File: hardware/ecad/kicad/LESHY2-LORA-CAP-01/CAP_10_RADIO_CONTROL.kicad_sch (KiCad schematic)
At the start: 0 parts

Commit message: complete H2.4.2 LoRa Cap root
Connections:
- no-connect marks 0 -> 10
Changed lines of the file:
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@@
 	(generator_version "10.0")
 	(paper "A4")
+	(hierarchical_label "CAP_3V3"
+		(shape bidirectional)
+		(at 20.32 20.32 0)
+		(effects (font (size 1.27 1.27)))
+	)
+	(wire
+		(pts (xy 20.32 20.32) (xy 25.40 20.32))
+		(stroke (width 0) (type default))
+	)
+	(no_connect (at 25.40 20.32)
+	)
+	(hierarchical_label "GND"
+		(shape bidirectional)
+		(at 20.32 25.40 0)
+		(effects (font (size 1.27 1.27)))
+	)
+	(wire
+		(pts (xy 20.32 25.40) (xy 25.40 25.40))
+		(stroke (width 0) (type default))
+	)
+	(no_connect (at 25.40 25.40)
+	)
+	(hierarchical_label "LORA_NRESET"
+		(shape bidirectional)
+		(at 20.32 30.48 0)
+		(effects (font (size 1.27 1.27)))
+	)
+	(wire
+		(pts (xy 20.32 30.48) (xy 25.40 30.48))
+		(stroke (width 0) (type default))
+	)
+	(no_connect (at 25.40 30.48)
+	)
+	(hierarchical_label "LORA_DIO1"
+		(shape bidirectional)
+		(at 20.32 35.56 0)
+		(effects (font (size 1.27 1.27)))
+	)
+	(wire
+		(pts (xy 20.32 35.56) (xy 25.40 35.56))
+		(stroke (width 0) (type default))
+	)
+	(no_connect (at 25.40 35.56)
+	)
+	(hierarchical_label "LORA_BUSY"
+		(shape bidirectional)
+		(at 20.32 40.64 0)
+		(effects (font (size 1.27 1.27)))
+	)
+	(wire
+		(pts (xy 20.32 40.64) (xy 25.40 40.64))
+		(stroke (width 0) (type default))
+	)
+	(no_connect (at 25.40 40.64)
+	)
+	(hierarchical_label "LORA_SCK"
+		(shape bidirectional)
+		(at 190.50 20.32 180)
+		(effects (font (size 1.27 1.27)) (justify right))
+	)
+	(wire
+		(pts (xy 190.50 20.32) (xy 185.42 20.32))
+		(stroke (width 0) (type default))
+	)
+	(no_connect (at 185.42 20.32)
+	)
+	(hierarchical_label "LORA_MOSI"
+		(shape bidirectional)
+		(at 190.50 25.40 180)
+		(effects (font (size 1.27 1.27)) (justify right))
+	)
+	(wire
+		(pts (xy 190.50 25.40) (xy 185.42 25.40))
+		(stroke (width 0) (type default))
+	)
+	(no_connect (at 185.42 25.40)
+	)
+	(hierarchical_label "LORA_MISO"
+		(shape bidirectional)
+		(at 190.50 30.48 180)
+		(effects (font (size 1.27 1.27)) (justify right))
+	)
+	(wire
+		(pts (xy 190.50 30.48) (xy 185.42 30.48))
+		(stroke (width 0) (type default))
+	)
+	(no_connect (at 185.42 30.48)
+	)
+	(hierarchical_label "LORA_NSS"
+		(shape bidirectional)
+		(at 190.50 35.56 180)
+		(effects (font (size 1.27 1.27)) (justify right))
+	)
+	(wire
+		(pts (xy 190.50 35.56) (xy 185.42 35.56))
+		(stroke (width 0) (type default))
+	)
+	(no_connect (at 185.42 35.56)
+	)
+	(hierarchical_label "RF_FORWARD_LEVEL"
+		(shape bidirectional)
+		(at 190.50 40.64 180)
+		(effects (font (size 1.27 1.27)) (justify right))
+	)
+	(wire
+		(pts (xy 190.50 40.64) (xy 185.42 40.64))
+		(stroke (width 0) (type default))
+	)
+	(no_connect (at 185.42 40.64)
+	)
 	(sheet_instances
 		(path "/"

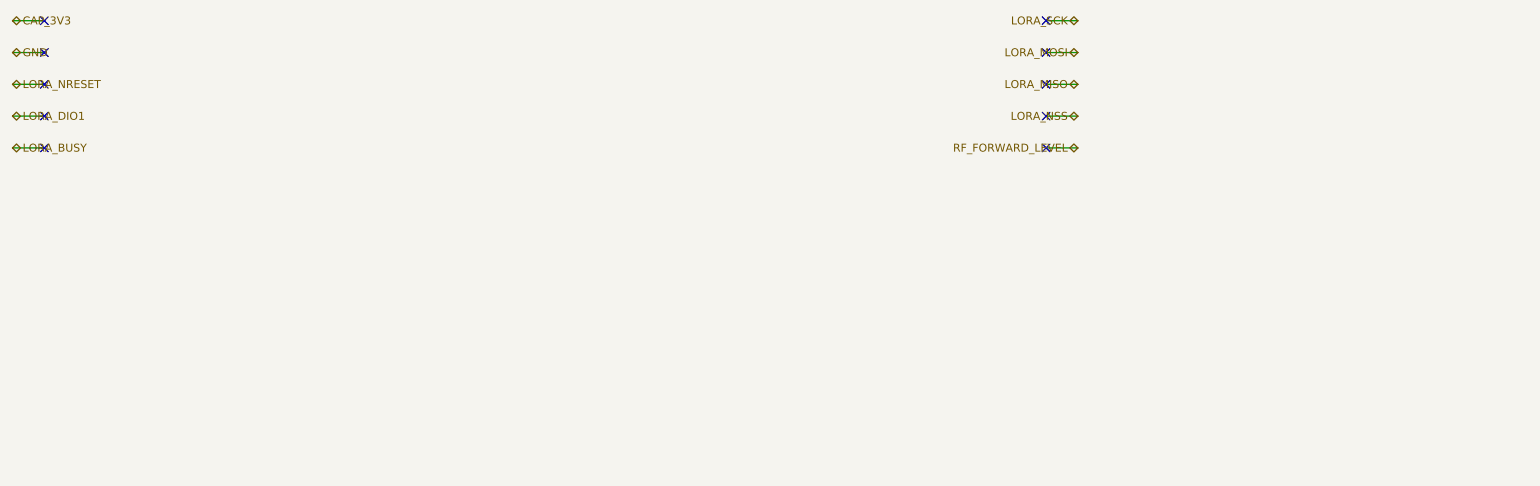
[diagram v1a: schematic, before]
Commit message: complete H2.4.3 LoRa radio path
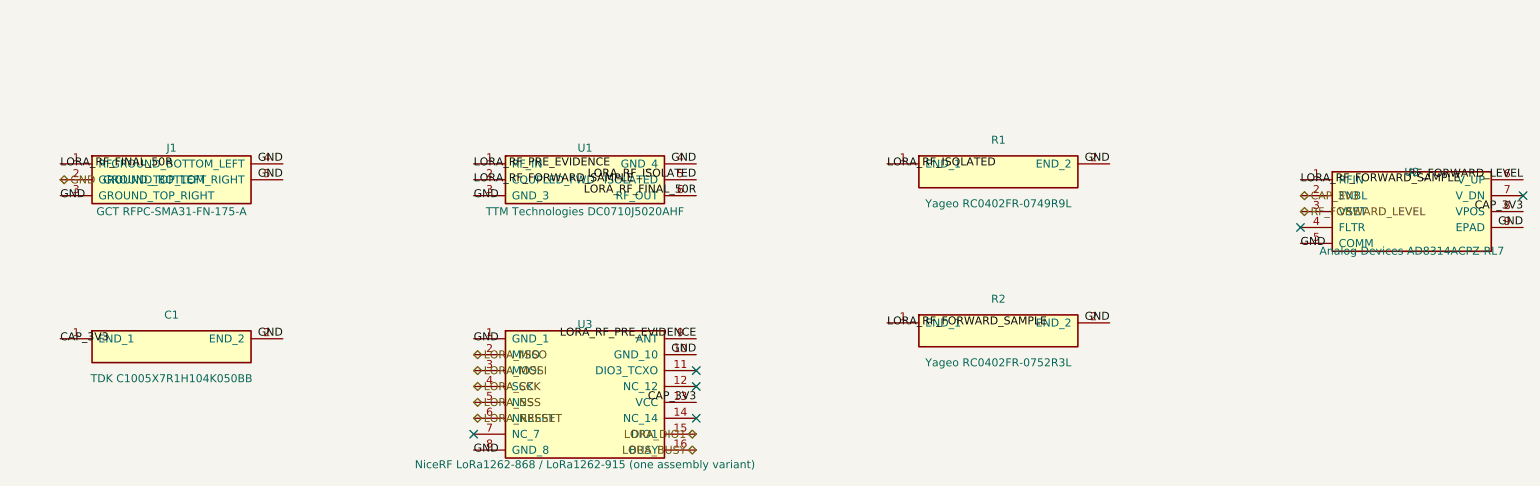
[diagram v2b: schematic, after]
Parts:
- added C1: TDK C1005X7R1H104K050BB, Capacitor_SMD:C_0402_1005Metric, symbol Leshy2:CAP10_RF_DETECTOR_BYPASS
- added J1: GCT RFPC-SMA31-FN-175-A, Leshy2:RFPC-SMA31-FN-175-A, symbol Leshy2:CAP10_RF_SMA
- added R1: Yageo RC0402FR-0749R9L, Resistor_SMD:R_0402_1005Metric, symbol Leshy2:CAP10_RF_ISOLATED_TERMINATION
- added R2: Yageo RC0402FR-0752R3L, Resistor_SMD:R_0402_1005Metric, symbol Leshy2:CAP10_RF_DETECTOR_MATCH
- added U1: TTM Technologies DC0710J5020AHF, Leshy2:DC0710J5020AHF, symbol Leshy2:CAP10_RF_COUPLER
- added U2: Analog Devices AD8314ACPZ-RL7, Package_CSP:LFCSP-8-1EP_3x2mm_P0.5mm_EP1.6x1.65mm, symbol Leshy2:CAP10_RF_DETECTOR
- added U3: NiceRF LoRa1262-868 / LoRa1262-915 (one assembly 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, Leshy2:NiceRF-LoRa126X, symbol Leshy2:CAP10_VARIANT_MODULE
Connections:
- net CAP_3V3: now also C1.1 (END_1), U2.2 (ENBL), U2.8 (VPOS), U3.13 (VCC)
- net GND: now also C1.2 (END_2), J1.2 (GROUND_TOP_LEFT), J1.3 (GROUND_TOP_RIGHT), J1.4 (GROUND_BOTTOM_LEFT), J1.5 (GROUND_BOTTOM_RIGHT), R1.2 (END_2), R2.2 (END_2), U1.3 (GND_3), U1.4 (GND_4), U2.5 (COMM), U2.9 (EPAD), U3.1 (GND_1), U3.10 (GND_10), U3.8 (GND_8)
- net LORA_BUSY: now also U3.16 (BUSY)
- net LORA_DIO1: now also U3.15 (DIO1)
- net LORA_MISO: now also U3.2 (MISO)
- net LORA_MOSI: now also U3.3 (MOSI)
- net LORA_NRESET: now also U3.6 (NRESET)
- net LORA_NSS: now also U3.5 (NSS)
- net LORA_SCK: now also U3.4 (SCK)
- net RF_FORWARD_LEVEL: now also U2.3 (VSET), U2.6 (V_UP)
- new net LORA_RF_FINAL_50R: J1.1 (RF), U1.6 (RF_OUT)
- new net LORA_RF_FORWARD_SAMPLE: R2.1 (END_1), U1.2 (COUPLED_FWD), U2.1 (RFIN)
- new net LORA_RF_ISOLATED: R1.1 (END_1), U1.5 (ISOLATED)
- new net LORA_RF_PRE_EVIDENCE: U1.1 (RF_IN), U3.9 (ANT)
- no-connect marks 10 -> 6
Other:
- title: (none) -> Leshy2 LoRa Cap — regional SX1262, final RF feed and forward-power detector

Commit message: complete H2 schematic review package
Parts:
- renumbered C1 to C10001, J1 to J10001, R1 to R10001, R2 to R10002, U1 to U10001, U2 to U10002, U3 to U10003
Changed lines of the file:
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@@
 		(on_board yes)
 		(dnp no)
-		(property "Reference" "J1"
+		(property "Reference" "J10001"
 			(at 45.72 40.64 0)
 			(show_name no)
@@
 			(project "LESHY2-LORA-CAP-01"
 				(path "/3e339712-8eb7-51c5-ac39-9e047a9dcb64"
-					(reference "J1")
+					(reference "J10001")
 					(unit 1)
 				)
@@
 		(on_board yes)
 		(dnp no)
-		(property "Reference" "U1"
+		(property "Reference" "U10001"
 			(at 111.76 40.64 0)
 			(show_name no)
@@
 			(project "LESHY2-LORA-CAP-01"
 				(path "/3e339712-8eb7-51c5-ac39-9e047a9dcb64"
-					(reference "U1")
+					(reference "U10001")
 					(unit 1)
 				)
@@
 		(on_board yes)
 		(dnp no)
-		(property "Reference" "R1"
+		(property "Reference" "R10001"
 			(at 177.80 39.37 0)
 			(show_name no)
@@
 			(project "LESHY2-LORA-CAP-01"
 				(path "/3e339712-8eb7-51c5-ac39-9e047a9dcb64"
-					(reference "R1")
+					(reference "R10001")
 					(unit 1)
 				)
@@
 		(on_board yes)
 		(dnp no)
-		(property "Reference" "U2"
+		(property "Reference" "U10002"
 			(at 243.84 44.50 0)
 			(show_name no)
@@
 			(project "LESHY2-LORA-CAP-01"
 				(path "/3e339712-8eb7-51c5-ac39-9e047a9dcb64"
-					(reference "U2")
+					(reference "U10002")
 					(unit 1)
 				)
@@
 		(on_board yes)
 		(dnp no)
-		(property "Reference" "R2"
+		(property "Reference" "R10002"
 			(at 177.80 64.77 0)
 			(show_name no)
@@
 			(project "LESHY2-LORA-CAP-01"
 				(path "/3e339712-8eb7-51c5-ac39-9e047a9dcb64"
-					(reference "R2")
+					(reference "R10002")
 					(unit 1)
 				)
@@
 		(on_board yes)
 		(dnp no)
-		(property "Reference" "C1"
+		(property "Reference" "C10001"
 			(at 45.72 67.31 0)
 			(show_name no)
@@
 			(project "LESHY2-LORA-CAP-01"
 				(path "/3e339712-8eb7-51c5-ac39-9e047a9dcb64"
-					(reference "C1")
+					(reference "C10001")
 					(unit 1)
 				)
@@
 		(on_board yes)
 		(dnp no)
-		(property "Reference" "U3"
+		(property "Reference" "U10003"
 			(at 111.76 68.81 0)
 			(show_name no)
@@
 			(project "LESHY2-LORA-CAP-01"
 				(path "/3e339712-8eb7-51c5-ac39-9e047a9dcb64"
-					(reference "U3")
-					(unit 1)
-				)
+					(reference "U10003")
+					(unit 1)
+				)

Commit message: Optimize H1 display and stocked BOM routes
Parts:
- C10001: value TDK C1005X7R1H104K050BB -> Yageo CC0402KRX7R9BB104
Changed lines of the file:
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@@
 			(effects (font (size 1.27 1.27)))
 		)
-		(property "Value" "TDK C1005X7R1H104K050BB"
+		(property "Value" "Yageo CC0402KRX7R9BB104"
 			(at 45.72 77.47 0)
 			(show_name no)
